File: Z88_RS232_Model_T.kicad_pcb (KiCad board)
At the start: 2 copper layers, 34.9 x 12 mm, 3 parts, among them J1 DE9_Male, J2 DB25 Female

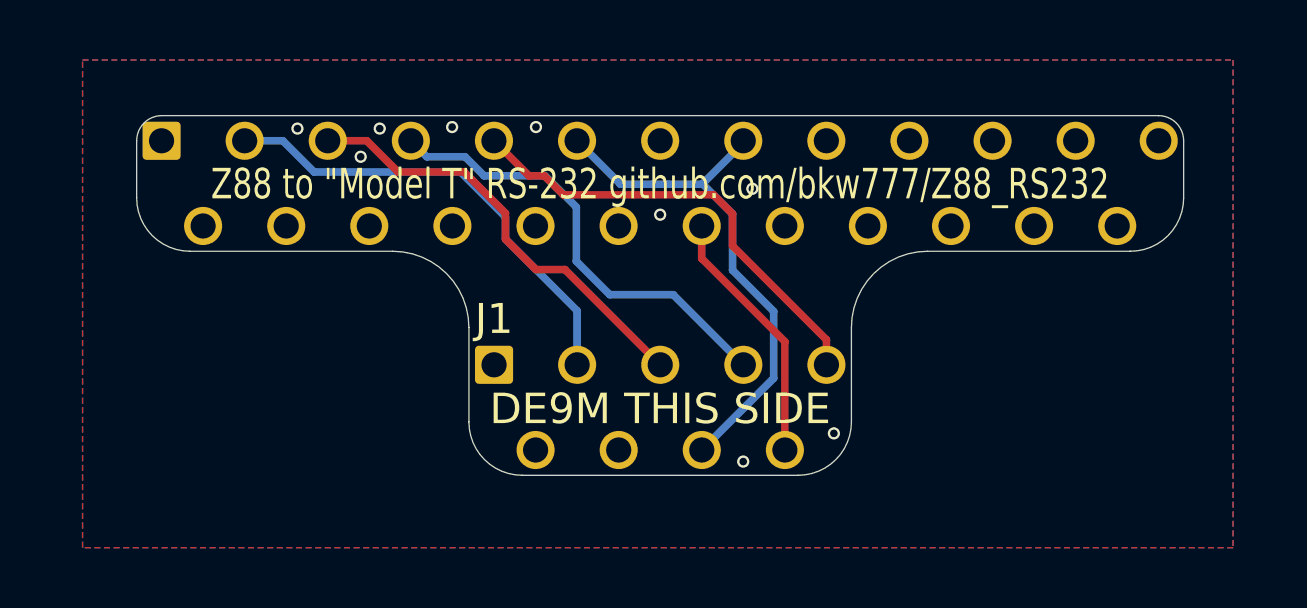
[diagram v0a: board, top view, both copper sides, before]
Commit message: kicad8, increase model-t pcb size
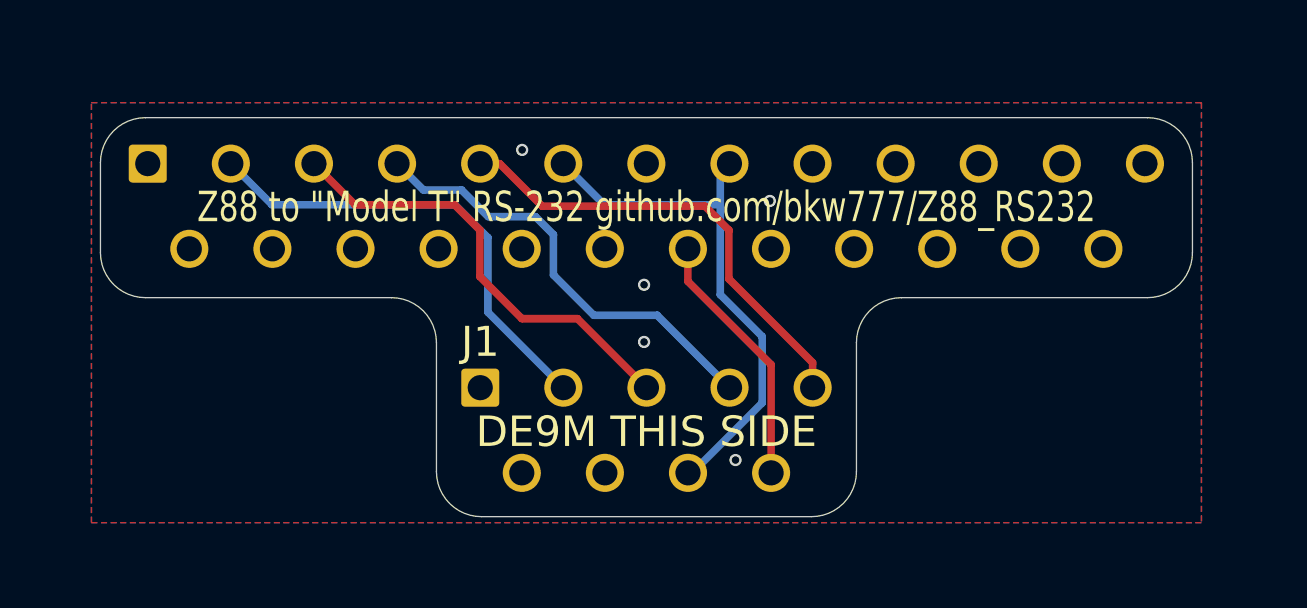
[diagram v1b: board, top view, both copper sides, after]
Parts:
- moved NT1 1.88 mm to (149.5, 90.4)
- moved J1 0.89 mm to (141.8, 96.5)
- moved J2 0.89 mm to (130.7, 89.1)
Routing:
- net /DSR: track 3.12 -> 5.29 mm
- net /DCD: track 14.0 -> 12.1 mm
- net GND: vias 9 -> 5
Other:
- board size 34.9 x 12 mm -> 36.4 x 13.3 mm
- net class Default removed
